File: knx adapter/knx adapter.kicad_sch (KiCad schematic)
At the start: 5 parts, among them J1 Conn_02x05_Odd_Even, J2 Conn_02x05_Odd_Even

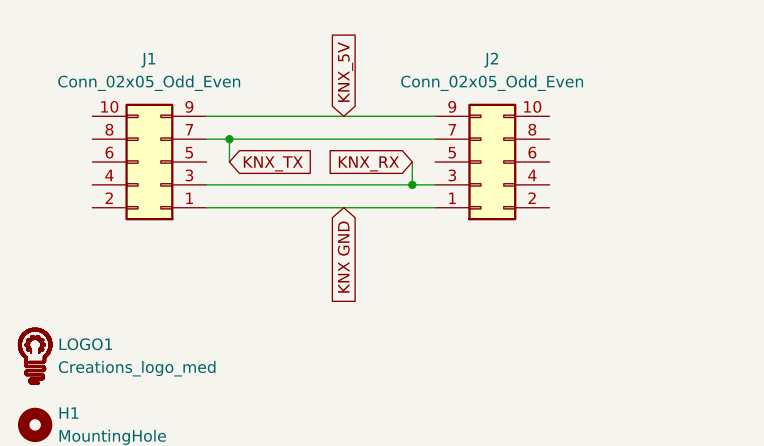
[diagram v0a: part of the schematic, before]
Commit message: update adapter to rev 002
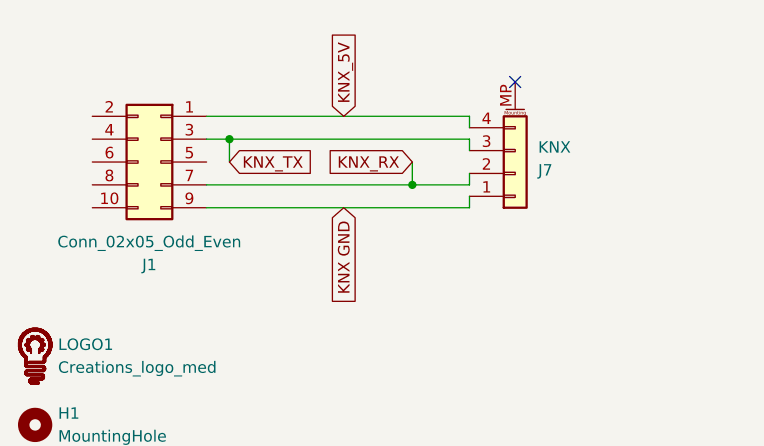
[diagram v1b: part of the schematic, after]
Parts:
- removed J2: Conn_02x05_Odd_Even, Connector_IDC:IDC-Header_2x05_P2.54mm_Vertical, symbol Connector_Generic:Conn_02x05_Odd_Even
- added J7: KNX, bare-footprints:4 pin jst 1.25 horizontal, symbol Connector_Generic_MountingPin:Conn_01x04_MountingPin
- H1, H2, LOGO1: now left out of the parts list
- J1: LCSC (none) -> C115170
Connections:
- net KNX GND: now also J1.9 (Pin_9), J7.1 (Pin_1); no longer J1.1 (Pin_1)
- net KNX_5V: now also J1.1 (Pin_1), J7.4 (Pin_4); no longer J1.9 (Pin_9)
- net KNX_RX: now also J1.7 (Pin_7), J7.2 (Pin_2); no longer J1.3 (Pin_3)
- net KNX_TX: now also J1.3 (Pin_3), J7.3 (Pin_3); no longer J1.7 (Pin_7)
- no-connect marks 0 -> 1
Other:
- moved on the sheet: J1
